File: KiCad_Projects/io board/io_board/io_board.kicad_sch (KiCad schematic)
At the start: 15 parts

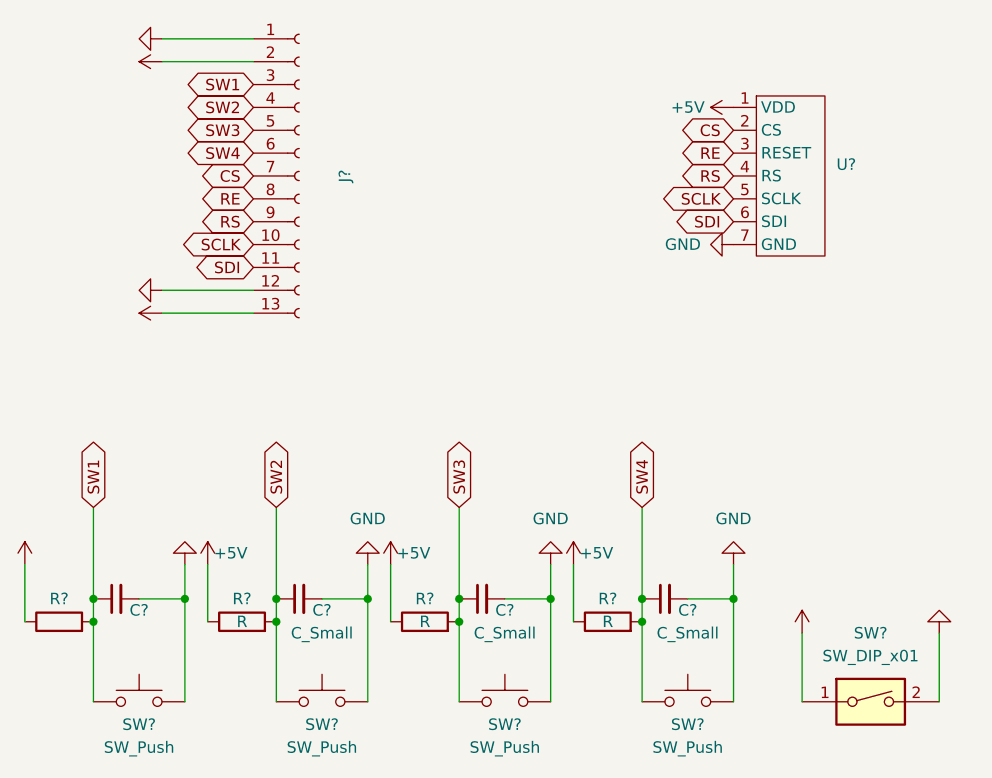
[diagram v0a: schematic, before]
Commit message: 基盤データの更新
電源基盤、IOボードの配線更新。
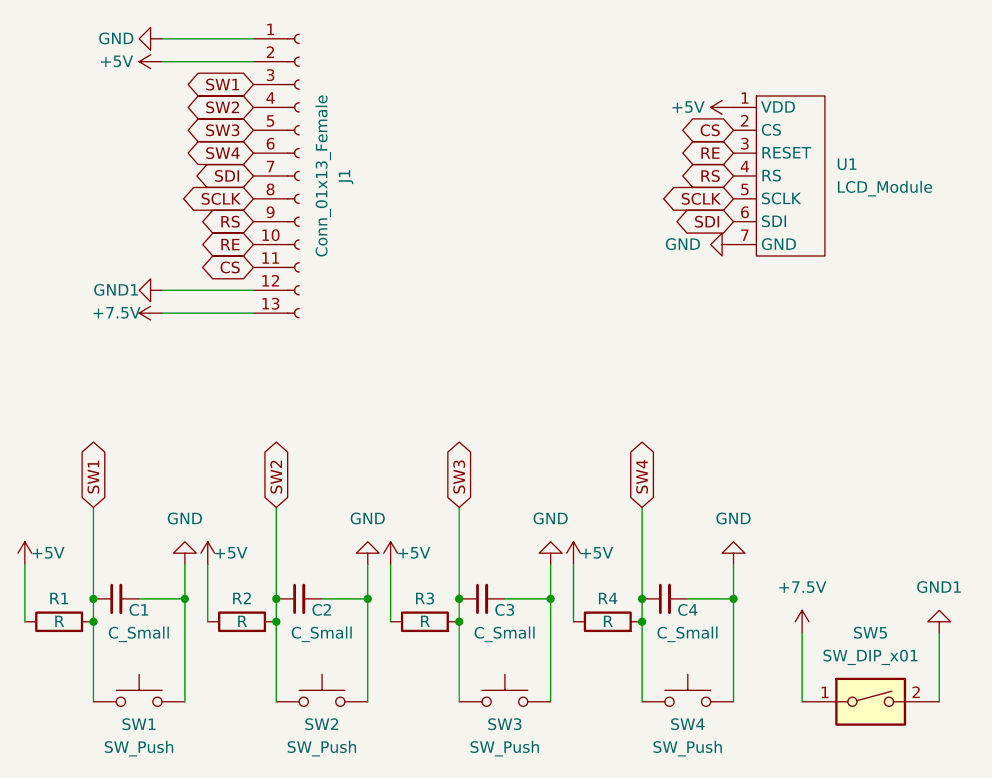
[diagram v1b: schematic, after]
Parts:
- C1: renamed from C?; value (none) -> C_Small
- J1: renamed from J?; value (none) -> Conn_01x13_Female
- R1: renamed from R?; value (none) -> R
- U1: renamed from U?; value (none) -> LCD_Module
- gave numbers to parts that had none: 11
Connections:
- net CS: now also J1.11 (Pin_11); no longer J1.7 (Pin_7)
- net RE: now also J1.10 (Pin_10); no longer J1.8 (Pin_8)
- net SCLK: now also J1.8 (Pin_8); no longer J1.10 (Pin_10)
- net SDI: now also J1.7 (Pin_7); no longer J1.11 (Pin_11)

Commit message: 部内大会用プログラムの作成
部内大会というか、北九州オープンくらいまでのプログラムが入ってます。
カメラ・IR_ring・Line_ringの制御。
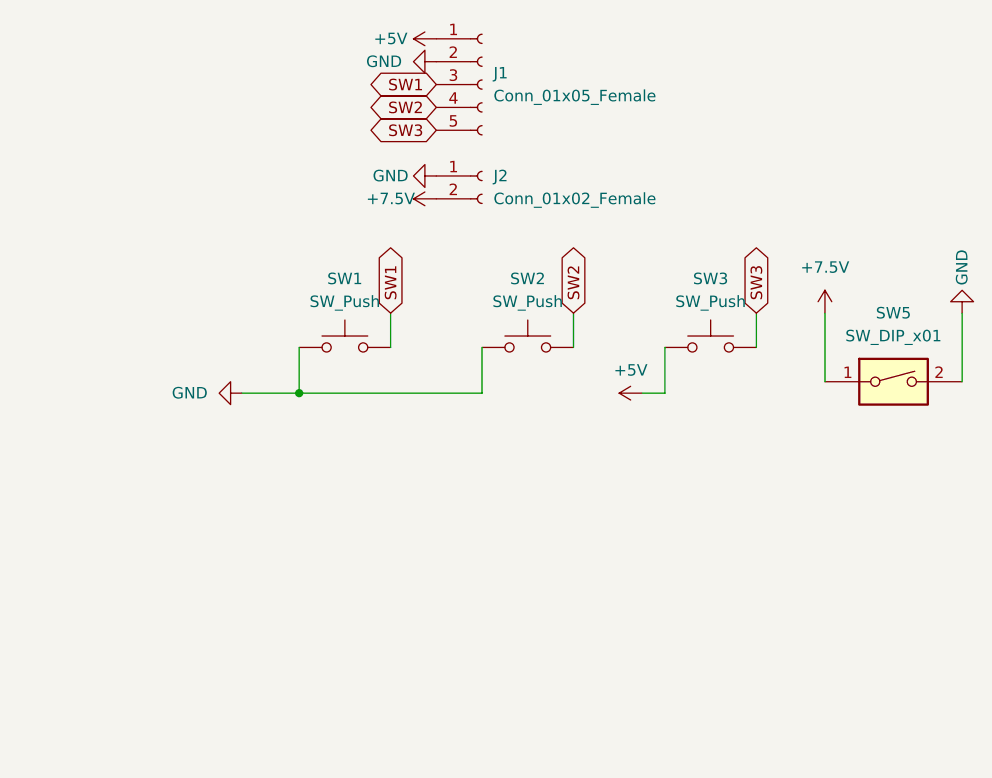
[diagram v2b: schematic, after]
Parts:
- removed C1, C2, C3, C4: C_Small, symbol Device:C_Small
- removed J1: Conn_01x13_Female, symbol Connector:Conn_01x13_Female
- removed R1, R2, R3, R4: R, symbol Device:R
- removed SW4: SW_Push, symbol Switch:SW_Push
- removed U1: LCD_Module, symbol LCD_Module_sym:LCD_Module
- added J1: Conn_01x05_Female, symbol Connector:Conn_01x05_Female
- added J2: Conn_01x02_Female, Connector_PinSocket_2.54mm:PinSocket_1x02_P2.54mm_Vertical, symbol Connector:Conn_01x02_Female
- SW1, SW2, SW3: footprint (none) -> Button_Switch_THT:SW_PUSH_6mm
- SW5: footprint (none) -> Lib:DS-850k
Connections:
- net GND1 is gone; now on net GND: SW5.2
- net +5V: now also SW3.1, J1.1 (Pin_1)
- net +7.5V: now also J2.2 (Pin_2)
- net GND: now also SW1.1, SW2.1, J1.2 (Pin_2), J2.1 (Pin_1); no longer SW1.2, SW2.2, SW3.2
- net SW1: now also SW1.2, J1.3 (Pin_3); no longer SW1.1
- net SW2: now also SW2.2, J1.4 (Pin_4); no longer SW2.1
- net SW3: now also SW3.2, J1.5 (Pin_5); no longer SW3.1
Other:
- moved on the sheet: SW1, SW2, SW3, SW5
